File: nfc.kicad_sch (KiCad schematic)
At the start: 36 parts, among them U4 ST25R3918AQW, Y1 27.12MHz

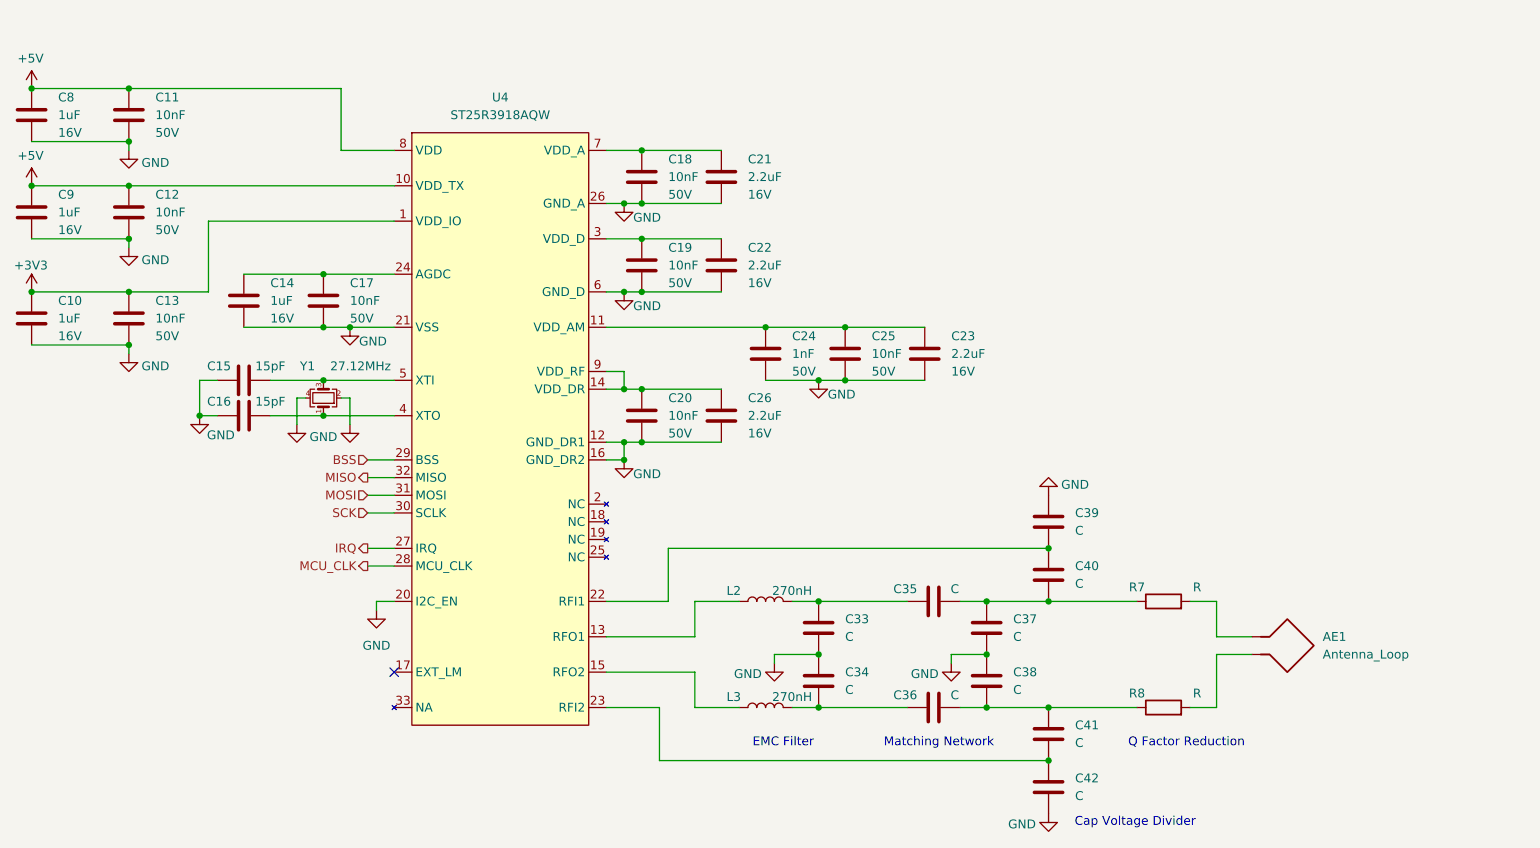
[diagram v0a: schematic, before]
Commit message: Replaced NFC reader IC with one available from JLCPCB.  Added matching circuit components from JLC Basic Parts library.  Modified syntax of antenna 3D model to fix loading issue
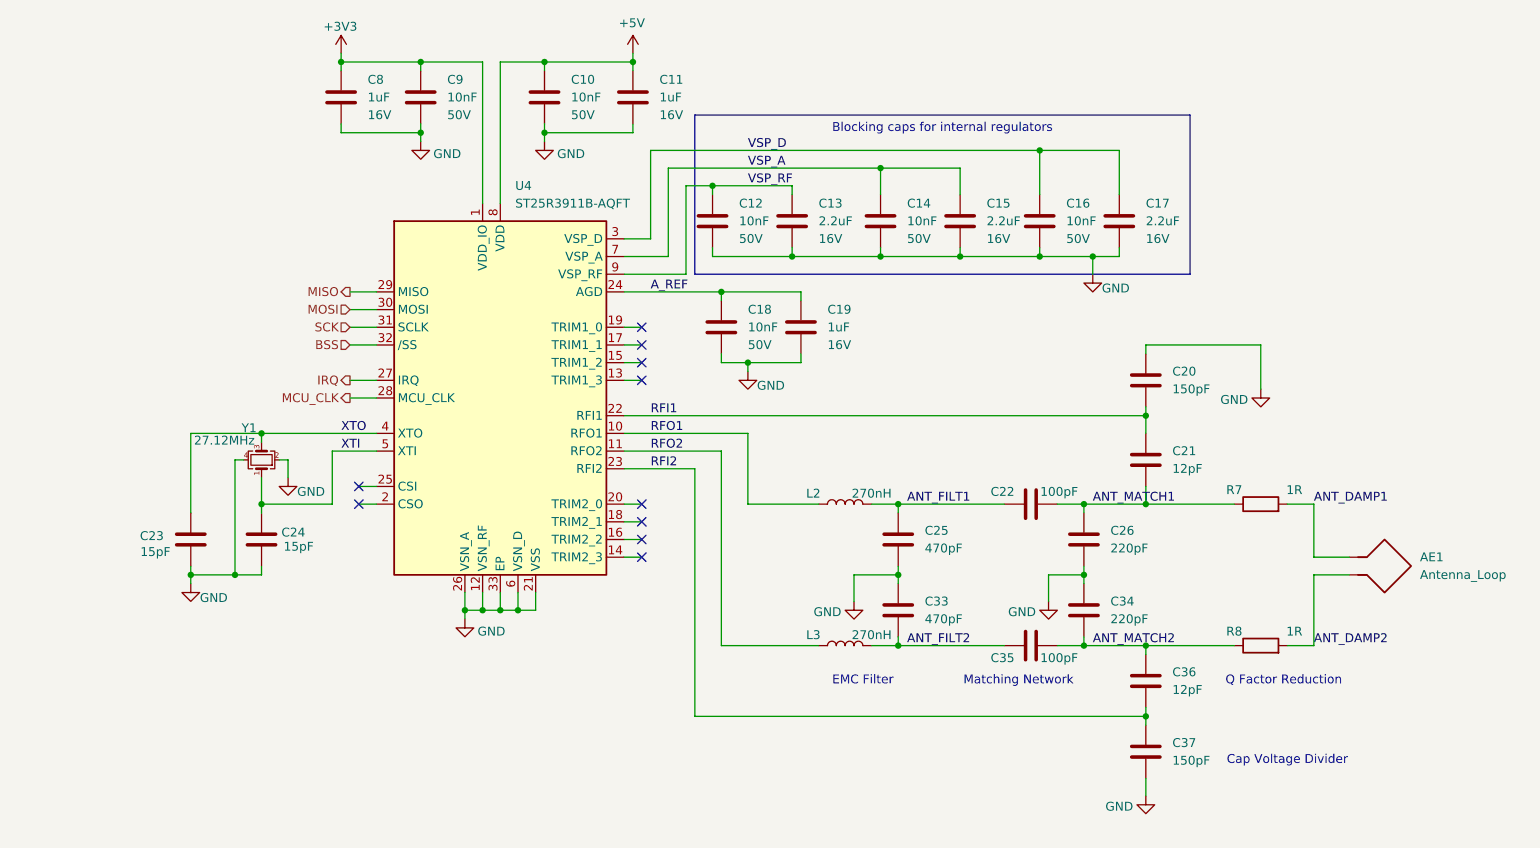
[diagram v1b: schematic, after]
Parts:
- removed C12, C25: 10nF, Capacitor_SMD:C_0603_1608Metric, symbol Device:C
- removed C23: 2.2uF, Capacitor_SMD:C_0603_1608Metric, symbol Device:C
- removed C24: 1nF, Capacitor_SMD:C_0603_1608Metric, symbol Device:C
- removed C38, C41, C42: C, Capacitor_SMD:C_0805_2012Metric, symbol Device:C
- removed C9: 1uF, Capacitor_SMD:C_0603_1608Metric, symbol Device:C
- removed U4: ST25R3918AQW, Package_DFN_QFN:HVQFN-32-1EP_5x5mm_P0.5mm_EP3.1x3.1mm, symbol parts:ST25R3918AQW
- added C26: 220pF, Capacitor_SMD:C_0805_2012Metric, symbol Device:C
- added C33: 470pF, Capacitor_SMD:C_0805_2012Metric, symbol Device:C
- added C35: 100pF, Capacitor_SMD:C_0805_2012Metric, symbol Device:C
- added U4: ST25R3911B-AQFT, Package_DFN_QFN:QFN-32-1EP_5x5mm_P0.5mm_EP3.6x3.6mm, symbol RF_NFC:ST25R3911B-AQF
- C20: renamed from C39; value C -> 150pF; LCSC Part # (none) -> C1716; MFPN (none) -> 0805B151K500NT; Voltage (none) -> 50V
- C21: renamed from C40; value C -> 12pF; LCSC Part # (none) -> C1792; MFPN (none) -> 0805CG120J500NT; Voltage (none) -> 50V
- C22: renamed from C35; value C -> 100pF; LCSC Part # (none) -> C1790; MFPN (none) -> CL21C101JBANNNC; Voltage (none) -> 50V
- C25: renamed from C33; value C -> 470pF; LCSC Part # (none) -> C1743; MFPN (none) -> 0805B471K500NT; Voltage (none) -> 50V
- C34: value C -> 220pF; LCSC Part # (none) -> C107145; MFPN (none) -> CC0805KRX7R9BB221; Voltage (none) -> 50V
- C36: value C -> 12pF; LCSC Part # (none) -> C1792; MFPN (none) -> 0805CG120J500NT; Voltage (none) -> 50V
- C37: value C -> 150pF; LCSC Part # (none) -> C1716; MFPN (none) -> 0805B151K500NT; Voltage (none) -> 50V
- L2, L3: DCR 500m -> 420m; LCSC Part # C107522 -> C723885; MFPN CI2012AR27K -> LQM21NNR27K10D
- R7, R8: value R -> 1R; LCSC Part # (none) -> C25271; MFPN (none) -> 0805W8F100KT5E
- Y1: LCSC Part # C70591 -> C5444554; MFPN X32252712MSB4SI -> XL2EL89CSI-111YLC-27.12M
- renumbered C11 to C10, C8 to C11, C18 to C12, C21 to C13, C19 to C14, C22 to C15, C20 to C16, C26 to C17, C17 to C18, C14 to C19, C15 to C23, C16 to C24, C10 to C8, C13 to C9
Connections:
- net +3V3: now also U4.1 (VDD_IO)
- net +5V: now also U4.8 (VDD)
- net BSS: now also U4.32 (/SS)
- net GND: now also C26.2, C33.1, U4.12 (VSN_RF), U4.21 (VSS), U4.26 (VSN_A), U4.33 (EP), U4.6 (VSN_D)
- net IRQ: now also U4.27 (IRQ)
- net MCU_CLK: now also U4.28 (MCU_CLK)
- net MISO: now also U4.29 (MISO)
- net MOSI: now also U4.30 (MOSI)
- net SCK: now also U4.31 (SCLK)
- net ANT_MATCH1: now reaches C21.2, C22.2, R7.1
- net ANT_MATCH1: now also C26.1; no longer C37.1
- net ANT_DAMP1: now reaches AE1.1, R7.2
- net XTI: now reaches C24.1, Y1.1
- net XTI: now also U4.5 (XTI)
- net XTO: now reaches C23.1, Y1.3
- net XTO: now also U4.4 (XTO)
- net RFI1: now reaches C20.2, C21.1
- net RFI1: now also U4.22 (RFI1)
- net VSP_A: now reaches C14.1, C15.2
- net VSP_A: now also U4.7 (VSP_A)
- net VSP_RF: now reaches C12.1, C13.2
- net VSP_RF: now also U4.9 (VSP_RF)
- net ANT_DAMP2: now reaches AE1.2, R8.2
- net ANT_FILT1: now reaches C22.1, C25.1, L2.2
- net ANT_MATCH2: now reaches C34.2, C36.1
- net ANT_MATCH2: now also R8.1, C35.2; no longer L3.2
- net RFI2: now reaches C36.2
- net RFI2: now also C37.1, U4.23 (RFI2); no longer R8.1
- net A_REF: now reaches C18.1, C19.1
- net A_REF: now also U4.24 (AGD)
- net VSP_D: now reaches C16.1, C17.2
- net VSP_D: now also U4.3 (VSP_D)
- net RFO1: now reaches L2.1
- net RFO1: now also U4.10 (RFO1)
- net RFO2: now reaches L3.1
- net RFO2: now also U4.11 (RFO2)
- new net ANT_FILT2: C33.2, C35.1, L3.2
- no-connect marks 1 -> 10
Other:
- moved on the sheet: AE1, C10, C11, C12, C13, C14, C15, C16, C17, C18, C19, C20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
